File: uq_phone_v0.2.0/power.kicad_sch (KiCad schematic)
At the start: 37 parts, among them J2 124018312112A, J3 BM03B-ACHSS-GAN-TF_LF__SN_, U1 TPS62162DSGR, U15 TPS22964CYZPR, U2 MCP73871-2CCI_ML, U3 BQ27441DRZR-G1A

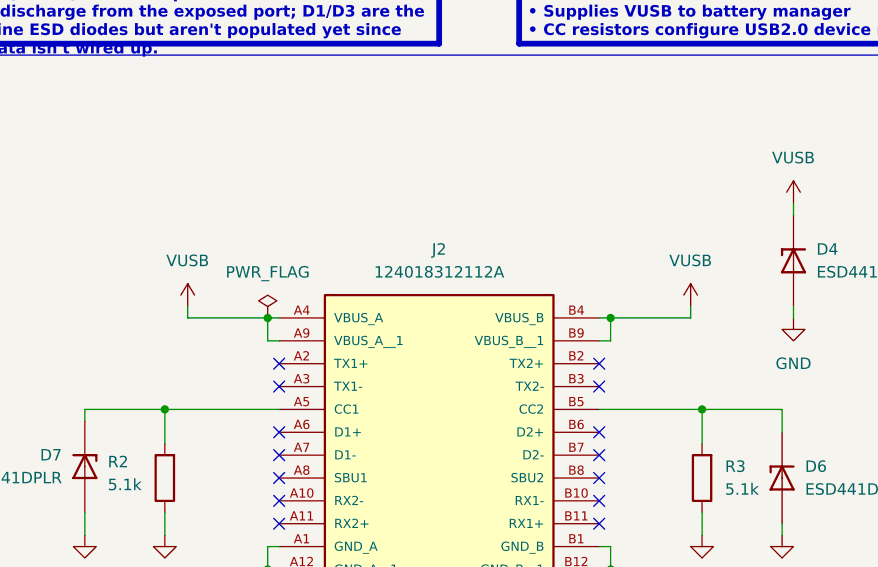
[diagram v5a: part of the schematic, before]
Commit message: Revert "Complete STM32H723ZGI6 144-pin schematic and FMC mapping"
This reverts commit c988dda79df5cbf87dce3ceded82a655262fe630.
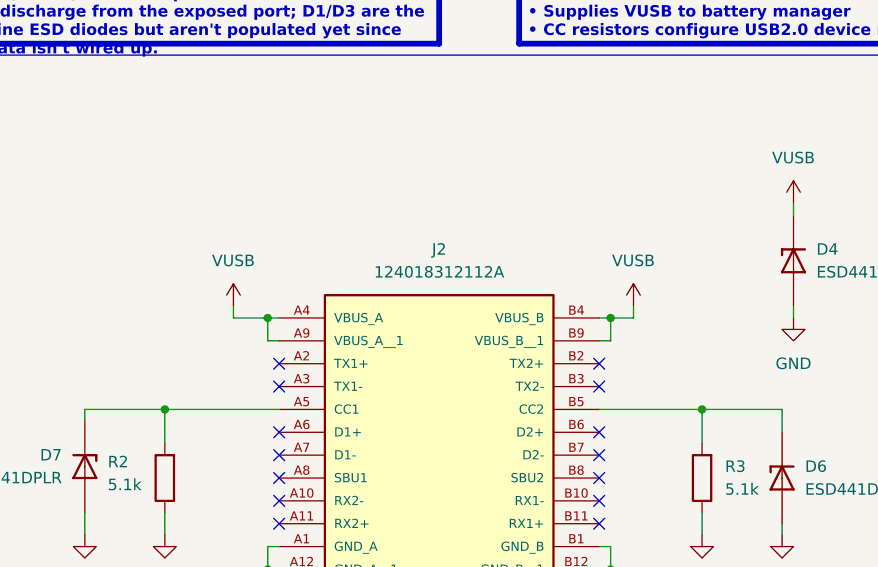
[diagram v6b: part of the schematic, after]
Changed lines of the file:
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@@
 	(wire
 		(pts
-			(xy 114.3 58.42) (xy 114.3 57.15)
+			(xy 107.95 58.42) (xy 107.95 57.15)
 		)
 		(stroke
@@
 	(wire
 		(pts
-			(xy 58.42 58.42) (xy 67.31 58.42)
+			(xy 63.5 58.42) (xy 67.31 58.42)
 		)
 		(stroke
@@
 	(wire
 		(pts
-			(xy 114.3 58.42) (xy 105.41 58.42)
+			(xy 107.95 58.42) (xy 105.41 58.42)
 		)
 		(stroke
@@
 	(wire
 		(pts
-			(xy 58.42 57.15) (xy 58.42 58.42)
+			(xy 63.5 57.15) (xy 63.5 58.42)
 		)
 		(stroke
@@
 	)
 	(symbol
-		(lib_id "power:PWR_FLAG")
-		(at 67.31 58.42 0)
-		(unit 1)
-		(exclude_from_sim no)
-		(in_bom yes)
-		(on_board yes)
-		(dnp no)
-		(fields_autoplaced yes)
-		(property "Reference" "#FLG01"
-			(at 67.31 56.515 0)
-			(effects
-				(font
-					(size 1.27 1.27)
-				)
-				(hide yes)
-			)
-		)
-		(property "Value" "PWR_FLAG"
-			(at 67.31 53.34 0)
-			(effects
-				(font
-					(size 1.27 1.27)
-				)
-			)
-		)
-		(property "Footprint" ""
-			(at 67.31 58.42 0)
-			(effects
-				(font
-					(size 1.27 1.27)
-				)
-				(hide yes)
-			)
-		)
-		(property "Datasheet" "~"
-			(at 67.31 58.42 0)
-			(effects
-				(font
-					(size 1.27 1.27)
-				)
-				(hide yes)
-			)
-		)
-		(property "Description" "Special symbol for telling ERC where power comes from"
-			(at 67.31 58.42 0)
-			(effects
-				(font
-					(size 1.27 1.27)
-				)
-				(hide yes)
-			)
-		)
-		(pin "1"
-		)
-		(instances
-			(project ""
-				(path "/14f57415-6807-40a5-bb38-3cb818a2cdae/e697a7f0-03cd-4a38-a369-080a37468a6a"
-					(reference "#FLG01")
-					(unit 1)
-				)
-			)
-		)
-	)
-	(symbol
 		(lib_id "power:VBUS")
 		(at 346.71 46.99 0)
@@
 	(symbol
 		(lib_id "power:VCC")
-		(at 114.3 57.15 0)
+		(at 107.95 57.15 0)
 		(unit 1)
 		(exclude_from_sim no)
@@
 		(fields_autoplaced yes)
 		(property "Reference" "#PWR07"
-			(at 114.3 60.96 0)
+			(at 107.95 60.96 0)
 			(effects
 				(font
@@
 		)
 		(property "Value" "VUSB"
-			(at 114.3 52.07 0)
+			(at 107.95 52.07 0)
 			(effects
 				(font
@@
 		)
 		(property "Footprint" ""
-			(at 114.3 57.15 0)
+			(at 107.95 57.15 0)
 			(effects
 				(font
@@
 		)
 		(property "Datasheet" ""
-			(at 114.3 57.15 0)
+			(at 107.95 57.15 0)
 			(effects
 				(font
@@
 		)
 		(property "Description" "Power symbol creates a global label with name \"VCC\""
-			(at 114.3 57.15 0)
+			(at 107.95 57.15 0)
 			(effects
 				(font
@@
 	(symbol
 		(lib_id "power:VCC")
-		(at 58.42 57.15 0)
+		(at 63.5 57.15 0)
 		(unit 1)
 		(exclude_from_sim no)
@@
 		(fields_autoplaced yes)
 		(property "Reference" "#PWR06"
-			(at 58.42 60.96 0)
+			(at 63.5 60.96 0)
 			(effects
 				(font
@@
 		)
 		(property "Value" "VUSB"
-			(at 58.42 52.07 0)
+			(at 63.5 52.07 0)
 			(effects
 				(font
@@
 		)
 		(property "Footprint" ""
-			(at 58.42 57.15 0)
+			(at 63.5 57.15 0)
 			(effects
 				(font
@@
 		)
 		(property "Datasheet" ""
-			(at 58.42 57.15 0)
+			(at 63.5 57.15 0)
 			(effects
 				(font
@@
 		)
 		(property "Description" "Power symbol creates a global label with name \"VCC\""
-			(at 58.42 57.15 0)
+			(at 63.5 57.15 0)
 			(effects
 				(font
